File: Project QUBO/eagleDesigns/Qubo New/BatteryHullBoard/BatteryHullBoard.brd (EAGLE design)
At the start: 53.3 x 39.7 mm, 8 parts, among them U1 KSK-1E66, U2 CMXSIPSSR

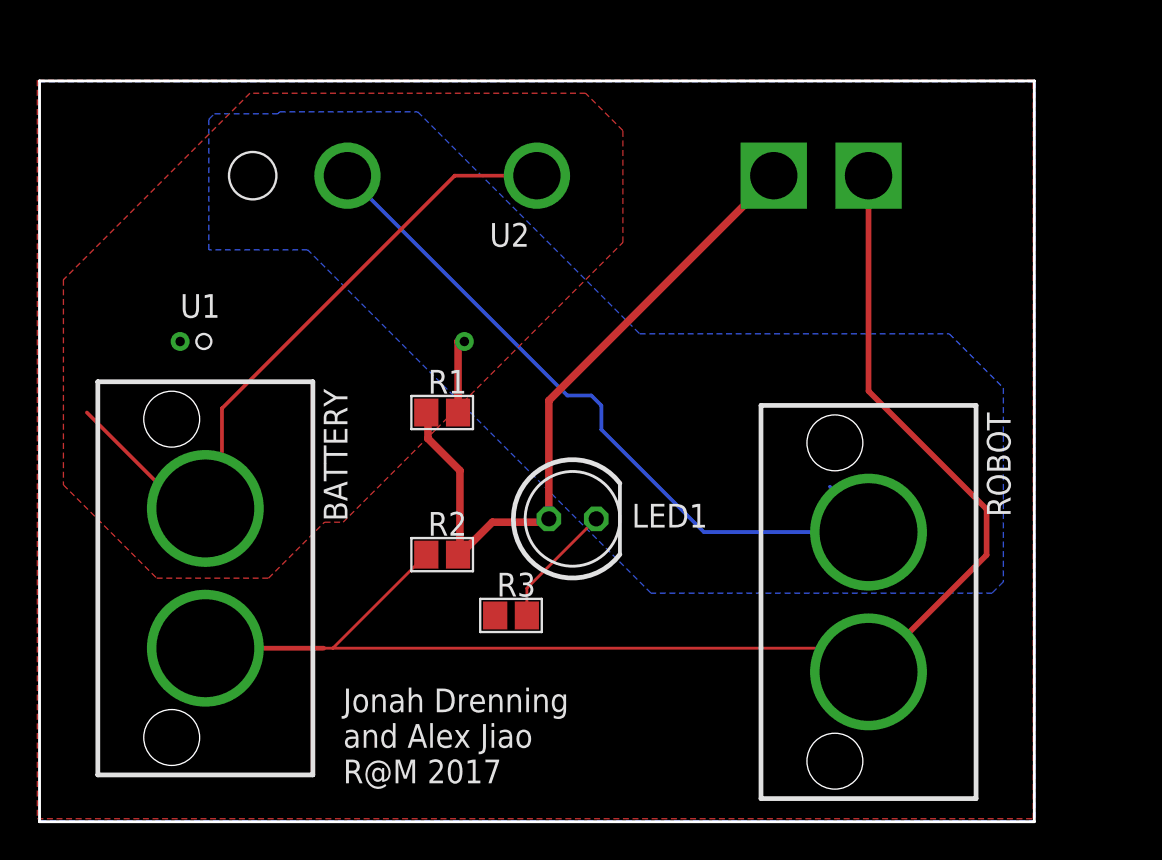
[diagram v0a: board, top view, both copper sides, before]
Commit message: Changed Relay on BatteryHubBoard with new one
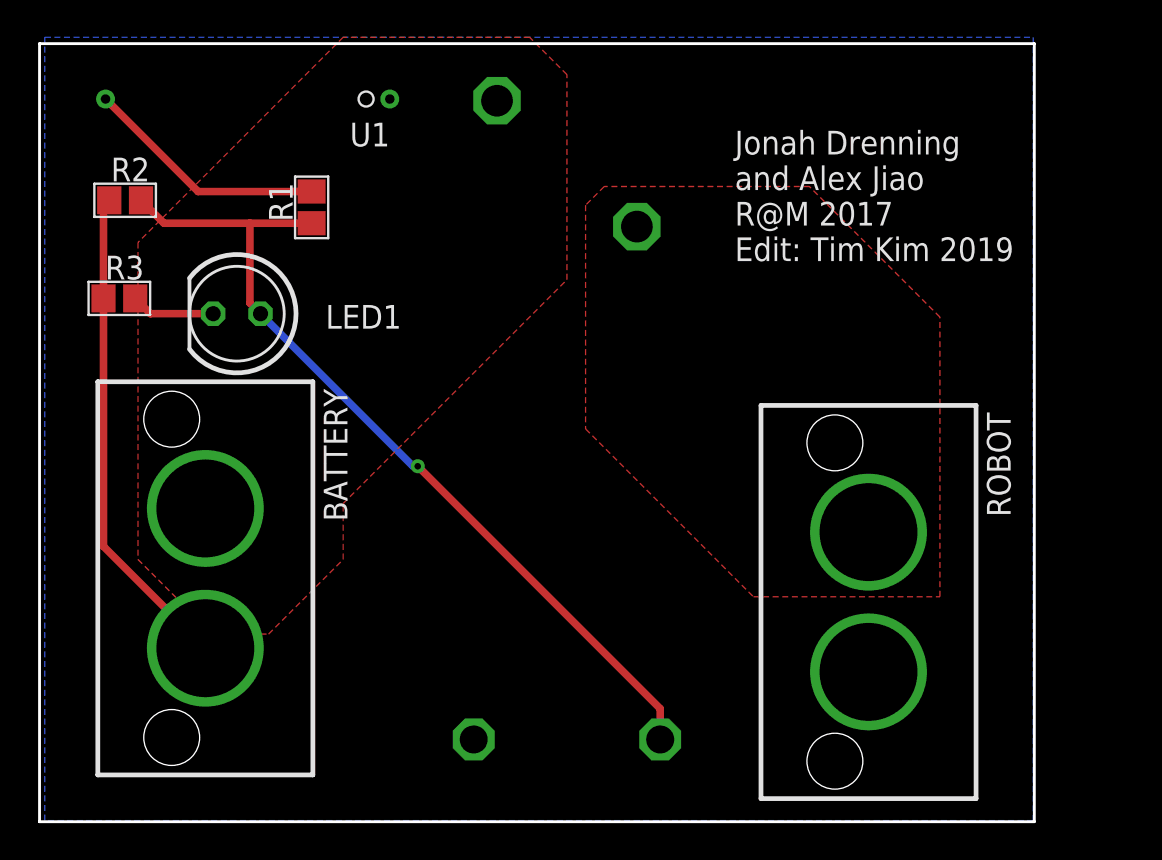
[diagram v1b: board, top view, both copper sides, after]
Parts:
- removed U2: CMXSIPSSR, CMXSIPSSR:CMXSIPSSR
- added U$1: ADJH21112, switch:ADJH21112
- moved R3 27.0 mm to (50.0, 62.0)
- moved R2 25.5 mm to (50.3, 67.3)
- moved LED1 21.1 mm to (56.3, 61.2), turned to 180 degrees
- moved U1 13.6 mm to (56.9, 72.7), turned to 180 degrees
- moved R1 13.0 mm to (60.3, 66.9), turned to 90 degrees
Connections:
- net GND: now also U$1.CONTROL-; no longer U2.P$4
- net N$3: now also U$1.CONRTOL+; no longer U2.P$3
- net PWR1: now also U$1.INPUT; no longer U2.P$2
- net PWR2: now also U$1.OUTPUT; no longer U2.P$1
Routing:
- net GND: track 75.1 -> 26.4 mm
- net PWR2: track 39.9 -> 0.00 mm
- net PWR1: track 36.3 -> 0.00 mm
- net N$3: track 37.4 -> 46.6 mm, vias 0 -> 1
- net N$1: track 4.15 -> 13.1 mm
- net N$4: track 6.72 -> 4.52 mm
- added copper zone on layer 16, net GND
- added copper zone on layer 1, net PWR2
- removed copper zone on layer 1, net GND
- removed copper zone on layer 16, net PWR2
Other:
- board size 53.3 x 39.7 mm -> 53.3 x 41.7 mm
- board text added: "Jonah Drenning and Alex Jiao R@M 2017 Edit: Tim Kim 2019"
- board text removed: "Jonah Drenning and Alex Jiao R@M 2017"
